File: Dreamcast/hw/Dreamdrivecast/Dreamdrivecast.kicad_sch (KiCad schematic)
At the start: 3 parts

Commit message: More notes about how the dreamcast gdrom protocol works and what the pins do
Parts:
- removed U?: Pico, RPi_Pico:RPi_Pico_SMD_TH, symbol MCU_RaspberryPi_and_Boards:Pico
- added U?: WeAct-RP2040-Pico, WeAct-RP2040-Pico:WeAct-RP2040-Pico, symbol Weact-RP2040-Pico:WeAct-RP2040-Pico
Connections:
- net D0: now also U?.1 (GP0)
- net D1: now also U?.2 (GP1)
- net D10: now also U?.14 (GP10)
- net D11: now also U?.15 (GP11)
- net D12: now also U?.16 (GP12)
- net D13: now also U?.17 (GP13)
- net D14: now also U?.19 (GP14)
- net D15: now also U?.20 (GP15)
- net D2: now also U?.4 (GP2)
- net D3: now also U?.5 (GP3)
- net D4: now also U?.6 (GP4)
- net D5: now also U?.7 (GP5)
- net D6: now also U?.9 (GP6)
- net D7: now also U?.10 (GP7)
- net D8: now also U?.11 (GP8)
- net D9: now also U?.12 (GP9)
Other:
- note added: "(audio data, serial)"
- note added: "33.8688 MHz"
- note added: "Bit clock"
- note added: "DMACK- (DMA acknowledge) (optional) This signal is used by the host in response to DMARQ, for initiating a DMA transfer. DMARQ- (DMA request) (optional) This signal is used for DMA transfer between the host and this device. When data transfer is possible, the device drives the signal. The data transfer direction is controlled by the DIOR- and DIOW- commands. This signal is used in handshaking wit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"
- note added: "D[0:15] Bidirectional data bus that can be used either as 8-bit or 16-bit bus."
- note added: "GD-ROM chip selection"
- note added: "IDE_CSO (Chip select 0) Serves for selecting the command block register. Note: This signal is known as "CS1FX-" in the industry. IDE_CS1(Chip select 1) Serves for selecting the control block register. Note: This signal is known as "CS3FX-" in the industry."
- note added: "INTRQ (Device interrupt) Serves for issuing an interrupt to the host. The INTRQ signal has a hold function which asserts the interrupt only when the device is selected and the host has cleared the nIEN bit in the device control register. When the nIEN bit is "1", or when the device is not selected, the INTRQ signal is in the high-impedance state, regardless of the presence of the hold interrupt. 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"
- note added: "IORDY (I/O channel ready) When the device cannot comply with a data transfer request, the signal is negated in order to expand the register access host transfer cycles. When this signal is driven, it is valid only during the DIOR-/DIOW- cycle for the selected device. When the IORDY signal is not negated, it is in the high- impedance state, because it is an open collector signal."
- note added: "Left right clock"
- note added: "RD (Read strobe signal from the host) At the falling edge of this signal, the data on the DDO- DD7, DD8-DD15 data bus from the device register or data port become valid. At the rising edge of this signal, the host latches on to the data. Until latching is completed, the host cannot access the data."
- note added: "RESET (Device reset) This signal is issued by the host. It is asserted at the start of power-on, and the assert state is maintained until the power supply level has stabilized. This is a tolerance interval until device reset after power-on. MCK (Main clock) 33.8688 MHz clock signal for AICA use. BCLK (Bit clock) Clock signal for fetching Digital Audio. LRCK (Left right clock) Digital Audio left/r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"
- note added: "Specifies the register and data read/write port."
- note added: "WR (Write strobe signal from the host) At the falling edge of this signal, the data on DDO- DD7, DD8-DD15 data bus from the device register or data port are latched. Until latching is completed, the device cannot access the data."
- note removed: "(33MHz)"
- note removed: "(audio data)"
- note removed: "CDDA What pins? Some pins are shared between ide and cdda?"
- note removed: "G1 Bus pins not used by GDRom. Used by Flash Memory?"
- moved on the sheet: CN?, JP?

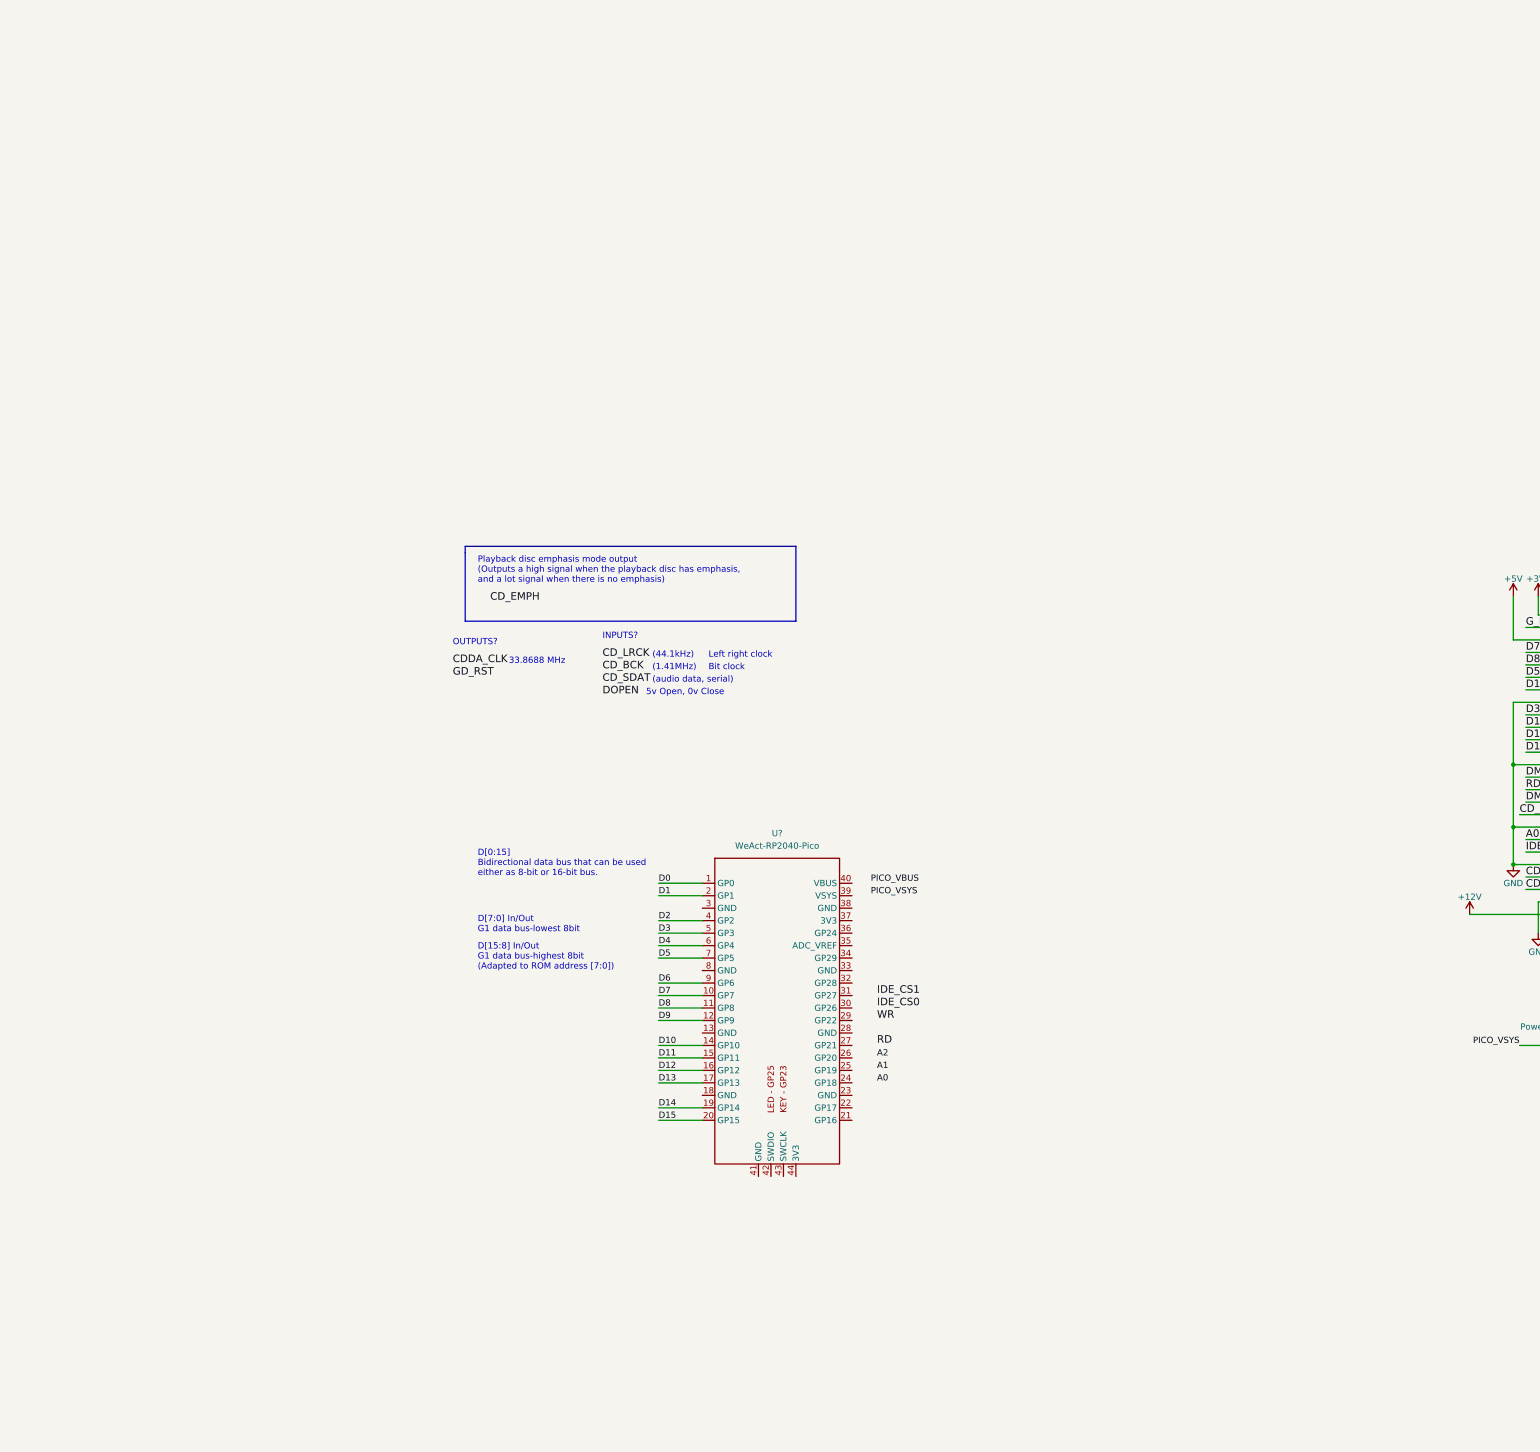
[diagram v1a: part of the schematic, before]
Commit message: Added possible two mcu approach to dreamcast dev board.
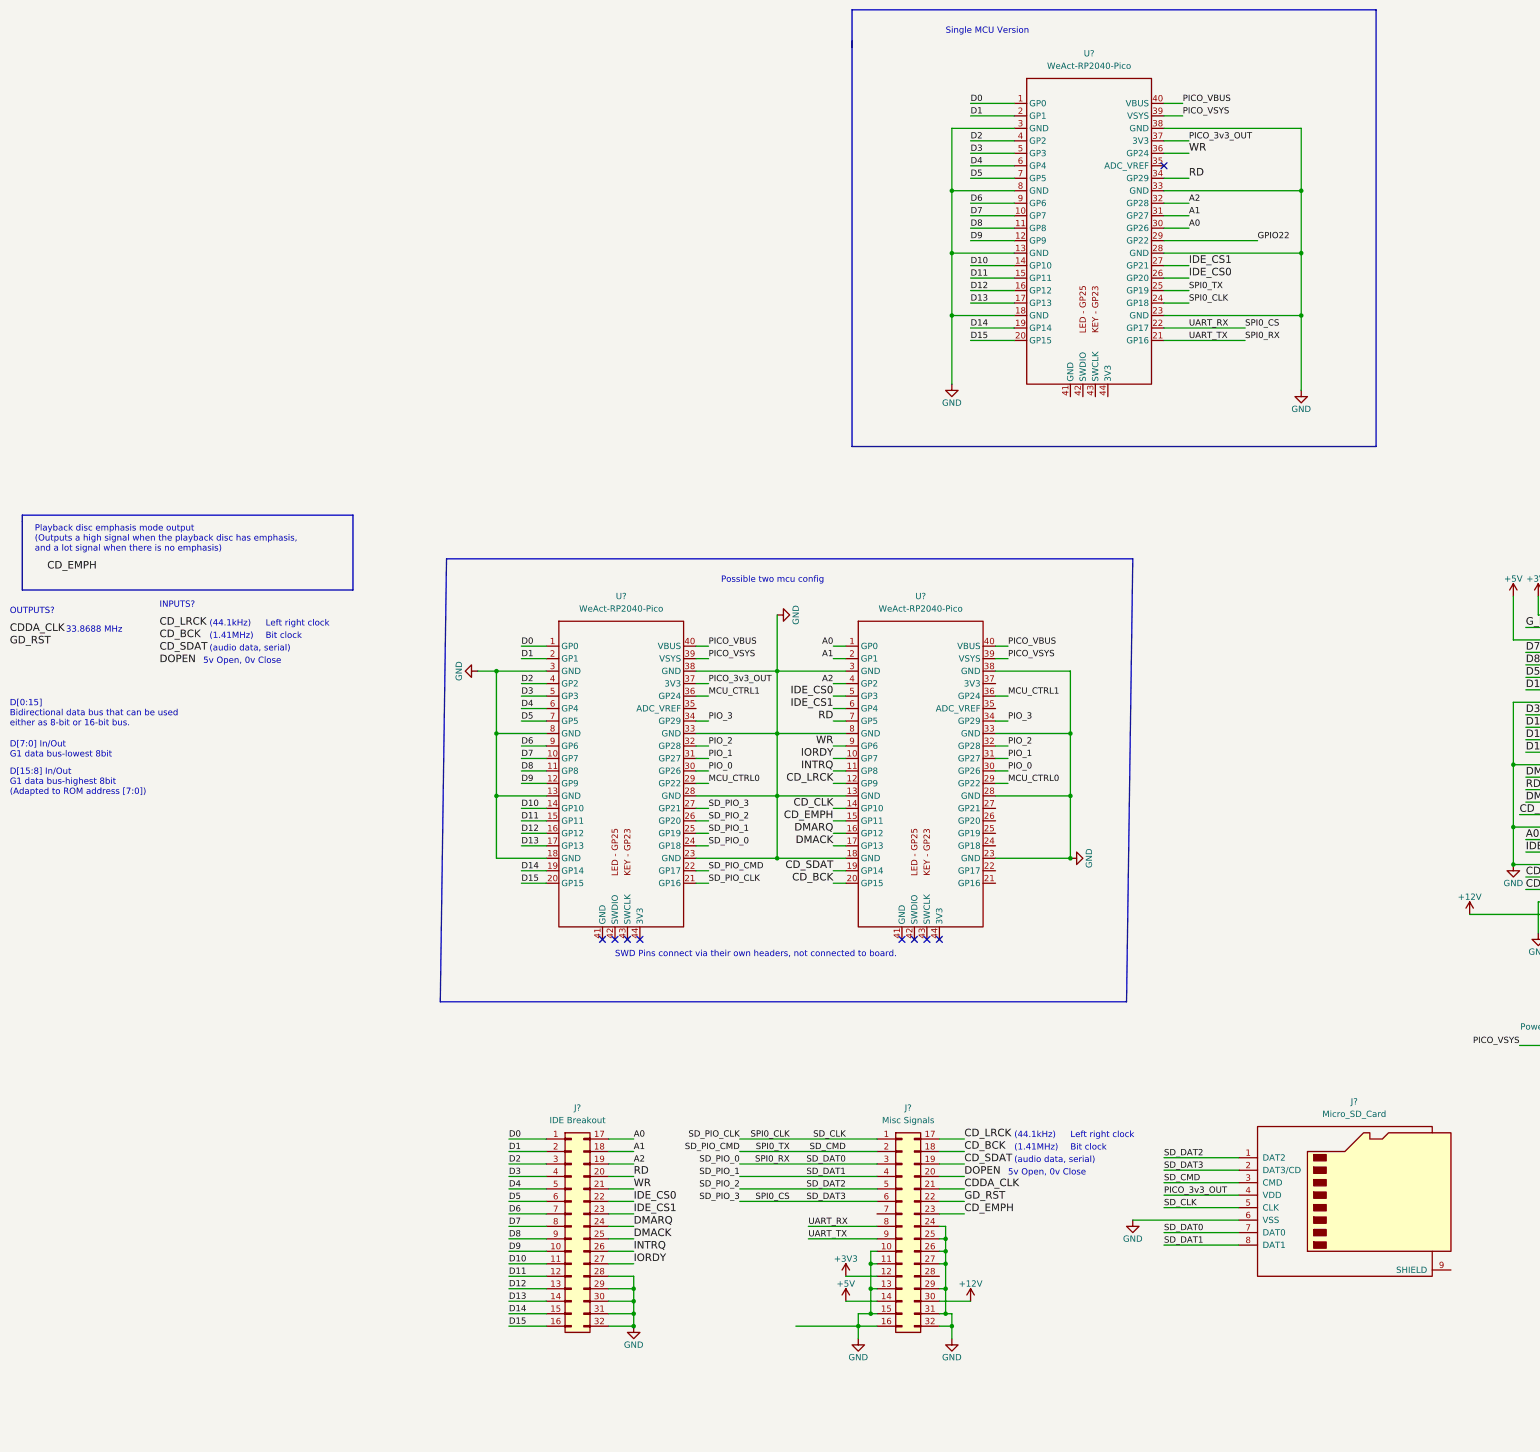
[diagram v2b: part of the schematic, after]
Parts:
- added J?: Misc Signals, symbol Connector_Generic:Conn_02x16_Top_Bottom
- added J?: IDE Breakout, symbol Connector_Generic:Conn_02x16_Top_Bottom
- added J?: Micro_SD_Card, symbol Connector:Micro_SD_Card
- added U? (x2): WeAct-RP2040-Pico, WeAct-RP2040-Pico:WeAct-RP2040-Pico, symbol Weact-RP2040-Pico:WeAct-RP2040-Pico
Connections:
- net +12V: now also J?.30 (Pin_30)
- net +3V3: now also J?.12 (Pin_12)
- net +5V: now also J?.14 (Pin_14)
- net A0: now also U?.30 (GP26), J?.17 (Pin_17), U?.1 (GP0)
- net A1: now also U?.31 (GP27), J?.18 (Pin_18), U?.2 (GP1)
- net A2: now also U?.32 (GP28), J?.19 (Pin_19), U?.4 (GP2)
- net CDDA_CLK: now also J?.21 (Pin_21)
- net CD_BCK: now also J?.18 (Pin_18), U?.20 (GP15)
- net CD_CLK: now also U?.14 (GP10)
- net CD_EMPH: now also J?.23 (Pin_23), U?.15 (GP11)
- net CD_LRCK: now also J?.17 (Pin_17), U?.12 (GP9)
- net CD_SDAT: now also J?.19 (Pin_19), U?.19 (GP14)
- net D0: now also J?.1 (Pin_1), U?.1 (GP0)
- net D1: now also J?.2 (Pin_2), U?.2 (GP1)
- net D10: now also J?.11 (Pin_11), U?.14 (GP10)
- net D11: now also J?.12 (Pin_12), U?.15 (GP11)
- net D12: now also J?.13 (Pin_13), U?.16 (GP12)
- net D13: now also J?.14 (Pin_14), U?.17 (GP13)
- net D14: now also J?.15 (Pin_15), U?.19 (GP14)
- net D15: now also J?.16 (Pin_16), U?.20 (GP15)
- net D2: now also J?.3 (Pin_3), U?.4 (GP2)
- net D3: now also J?.4 (Pin_4), U?.5 (GP3)
- net D4: now also J?.5 (Pin_5), U?.6 (GP4)
- net D5: now also J?.6 (Pin_6), U?.7 (GP5)
- net D6: now also J?.7 (Pin_7), U?.9 (GP6)
- net D7: now also J?.8 (Pin_8), U?.10 (GP7)
- net D8: now also J?.9 (Pin_9), U?.11 (GP8)
- net D9: now also J?.10 (Pin_10), U?.12 (GP9)
- net DMACK: now also J?.25 (Pin_25), U?.17 (GP13)
- net DMARQ: now also J?.24 (Pin_24), U?.16 (GP12)
- net DOPEN: now also J?.20 (Pin_20)
- net GD_RST: now also J?.22 (Pin_22)
- net GND: now also U?.13 (GND), U?.18 (GND), U?.23 (GND), U?.28 (GND), U?.3 (GND), U?.33 (GND), U?.38 (GND), U?.8 (GND), J?.10 (Pin_10), J?.11 (Pin_11), J?.13 (Pin_13), J?.15 (Pin_15), J?.16 (Pin_16), J?.24 (Pin_24), J?.25 (Pin_25), J?.26 (Pin_26), J?.27 (Pin_27), J?.28 (Pin_28), J?.29 (Pin_29), J?.29 (Pin_29), J?.30 (Pin_30), J?.31 (Pin_31), J?.31 (Pin_31), J?.32 (Pin_32), J?.32 (Pin_32), J?.6 (VSS), U?.13 (GND), U?.13 (GND), U?.18 (GND), U?.18 (GND), U?.23 (GND), U?.23 (GND), U?.28 (GND), U?.28 (GND), U?.3 (GND), U?.3 (GND), U?.33 (GND), U?.33 (GND), U?.38 (GND), U?.38 (GND), U?.8 (GND), U?.8 (GND)
- net IDE_CS0: now also U?.26 (GP20), J?.22 (Pin_22), U?.5 (GP3)
- net IDE_CS1: now also U?.27 (GP21), J?.23 (Pin_23), U?.6 (GP4)
- net INTRQ: now also J?.26 (Pin_26), U?.11 (GP8)
- net IORDY: now also J?.27 (Pin_27), U?.10 (GP7)
- net PICO_VBUS: now also U?.40 (VBUS), U?.40 (VBUS), U?.40 (VBUS)
- net PICO_VSYS: now also U?.39 (VSYS), U?.39 (VSYS), U?.39 (VSYS)
- net RD: now also U?.34 (GP29), J?.20 (Pin_20), U?.7 (GP5)
- net WR: now also U?.36 (GP24), J?.21 (Pin_21), U?.9 (GP6)
- net SD_DAT0: now reaches U?.21 (GP16)
- net SD_DAT0: now also J?.3 (Pin_3), J?.7 (DAT0), J?.9 (Pin_9), U?.24 (GP18)
- net SD_DAT3: now reaches U?.22 (GP17)
- net SD_DAT3: now also J?.2 (DAT3/CD), J?.6 (Pin_6), J?.8 (Pin_8), U?.27 (GP21)
- net SD_CLK: now reaches U?.24 (GP18)
- net SD_CLK: now also J?.1 (Pin_1), J?.5 (CLK), U?.21 (GP16)
- net SD_CMD: now reaches U?.25 (GP19)
- net SD_CMD: now also J?.2 (Pin_2), J?.3 (CMD), U?.22 (GP17)
- net GPIO22: now reaches U?.29 (GP22)
- net PICO_3v3_OUT: now reaches U?.37 (3V3)
- net PICO_3v3_OUT: now also J?.4 (VDD), U?.37 (3V3)
- new net MCU_CTRL0: U?.29 (GP22), U?.29 (GP22)
- new net MCU_CTRL1: U?.36 (GP24), U?.36 (GP24)
- new net PIO_0: U?.30 (GP26), U?.30 (GP26)
- new net PIO_1: U?.31 (GP27), U?.31 (GP27)
- new net PIO_2: U?.32 (GP28), U?.32 (GP28)
- new net PIO_3: U?.34 (GP29), U?.34 (GP29)
- new net SD_DAT1: J?.4 (Pin_4), J?.8 (DAT1), U?.25 (GP19)
- new net SD_DAT2: J?.1 (DAT2), J?.5 (Pin_5), U?.26 (GP20)
- no-connect marks 0 -> 9
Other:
- note added: "Possible two mcu config"
- note added: "SWD Pins connect via their own headers, not connected to board."
- note added: "Single MCU Version"
- moved on the sheet: U?

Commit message: Ignore the backup folder. AND also check in the changes to the schematic.
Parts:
- removed U?: WeAct-RP2040-Pico, WeAct-RP2040-Pico:WeAct-RP2040-Pico, symbol Weact-RP2040-Pico:WeAct-RP2040-Pico
- added J?: Ground Block, symbol Connector:Conn_01x16_Male
- added R?: R, Resistor_THT:R_Axial_DIN0207_L6.3mm_D2.5mm_P5.08mm_Vertical, symbol db-passives:R
- added SW?: Lid, symbol Switch:SW_SPST
- JP?: value Power from Dreamcast -> Use Dreamcast Power
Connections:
- net +3V3: now also J?.28 (Pin_28); no longer J?.12 (Pin_12)
- net +5V: now also J?.26 (Pin_26), R?.1; no longer J?.14 (Pin_14)
- net DOPEN: now also R?.2, SW?.2 (B)
- net GND: now also J?.7 (Pin_7), J?.9 (SHIELD), J?.1 (Pin_1), J?.10 (Pin_10), J?.11 (Pin_11), J?.12 (Pin_12), J?.13 (Pin_13), J?.14 (Pin_14), J?.15 (Pin_15), J?.16 (Pin_16), J?.2 (Pin_2), J?.3 (Pin_3), J?.4 (Pin_4), J?.5 (Pin_5), J?.6 (Pin_6), J?.7 (Pin_7), J?.8 (Pin_8), J?.9 (Pin_9), SW?.1 (A); no longer J?.10 (Pin_10), J?.11 (Pin_11), J?.13 (Pin_13), J?.24 (Pin_24), J?.25 (Pin_25), J?.26 (Pin_26), J?.27 (Pin_27), J?.29 (Pin_29), J?.31 (Pin_31)
- net MCU_CTRL0: now also J?.11 (Pin_11)
- net MCU_CTRL1: now also J?.12 (Pin_12)
- net SD_DAT0: no longer J?.9 (Pin_9)
- net SD_DAT3: no longer J?.8 (Pin_8)
- net MCU2_UART_TX: now reaches U?.21 (GP16)
- net MCU2_UART_TX: now also J?.9 (Pin_9)
- net MCU2_UART_RX: now reaches U?.22 (GP17)
- net MCU2_UART_RX: now also J?.8 (Pin_8)
- no-connect marks 9 -> 23
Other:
- note added: "2023-02-16"
- note added: "GDROM Breakout Devboard"
- note added: "GDROM Lid Switch"
- note added: "Power Picos from Dreamcast"
- note removed: "Possible two mcu config"
- note removed: "Single MCU Version"
- moved on the sheet: CN?, J?, JP?, U?

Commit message: Routed dreamcast board. Added some footprints and symbols for the molex connector.
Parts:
- removed J?: Misc Signals, symbol Connector_Generic:Conn_02x16_Top_Bottom
- removed J?: IDE Breakout, symbol Connector_Generic:Conn_02x16_Top_Bottom
- removed J?: Ground Block, symbol Connector:Conn_01x16_Male
- added J1: Breakout, Connector_PinHeader_2.54mm:PinHeader_2x25_P2.54mm_Vertical_SMD, symbol Connector_Generic:Conn_02x25_Top_Bottom
- added J2: POWER, Connector_PinHeader_2.54mm:PinHeader_1x05_P2.54mm_Vertical, symbol Connector:Conn_01x05_Male
- CN1: renamed from CN?; footprint Molex_52602_0579:Molex_52602_0579 -> riser:Molex_52602_0579
- J4: renamed from J?; footprint (none) -> Connector_Card:microSD_HC_Molex_104031-0811
- JP1: renamed from JP?; footprint (none) -> Jumper:SolderJumper-2_P1.3mm_Open_RoundedPad1.0x1.5mm
- SW1: renamed from SW?; footprint (none) -> Button_Switch_THT:SW_DIP_SPSTx01_Slide_9.78x4.72mm_W7.62mm_P2.54mm
- gave numbers to parts that had none: 3
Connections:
- net +12V: now also J2.5 (Pin_5)
- net +3V3: now also J2.4 (Pin_4)
- net +5V: now also J2.3 (Pin_3)
- net A0: now also J1.17 (Pin_17)
- net A1: now also J1.18 (Pin_18)
- net A2: now also J1.19 (Pin_19)
- net CDDA_CLK: now also J1.32 (Pin_32)
- net CD_BCK: now also J1.29 (Pin_29)
- net CD_EMPH: now also J1.34 (Pin_34)
- net CD_LRCK: now also J1.28 (Pin_28)
- net CD_SDAT: now also J1.30 (Pin_30)
- net D0: now also J1.1 (Pin_1)
- net D1: now also J1.2 (Pin_2)
- net D10: now also J1.11 (Pin_11)
- net D11: now also J1.12 (Pin_12)
- net D12: now also J1.13 (Pin_13)
- net D13: now also J1.14 (Pin_14)
- net D14: now also J1.15 (Pin_15)
- net D15: now also J1.16 (Pin_16)
- net D2: now also J1.3 (Pin_3)
- net D3: now also J1.4 (Pin_4)
- net D4: now also J1.5 (Pin_5)
- net D5: now also J1.6 (Pin_6)
- net D6: now also J1.7 (Pin_7)
- net D7: now also J1.8 (Pin_8)
- net D8: now also J1.9 (Pin_9)
- net D9: now also J1.10 (Pin_10)
- net DMACK: now also J1.25 (Pin_25)
- net DMARQ: now also J1.24 (Pin_24)
- net DOPEN: now also J1.31 (Pin_31)
- net GD_RST: now also J1.33 (Pin_33)
- net GND: now also J1.35 (Pin_35), J1.36 (Pin_36), J1.37 (Pin_37), J1.38 (Pin_38), J1.39 (Pin_39), J1.40 (Pin_40), J2.1 (Pin_1); no longer U1.13 (GND), U1.18 (GND), U1.3 (GND), U1.8 (GND), U2.23 (GND), U2.28 (GND), U2.33 (GND), U2.38 (GND)
- net IDE_CS0: now also J1.22 (Pin_22)
- net IDE_CS1: now also J1.23 (Pin_23)
- net INTRQ: now also J1.26 (Pin_26)
- net IORDY: now also J1.27 (Pin_27)
- net MCU2_UART_RX: now also J1.41 (Pin_41)
- net MCU2_UART_TX: now also J1.42 (Pin_42)
- net MCU_CTRL0: now also J1.43 (Pin_43)
- net MCU_CTRL1: now also J1.44 (Pin_44)
- net PICO_3v3_OUT: now also J2.2 (Pin_2)
- net RD: now also J1.20 (Pin_20)
- net SD_CLK: now also J1.45 (Pin_45); no longer U1.21 (GP16)
- net SD_CMD: now also J1.46 (Pin_46); no longer U1.22 (GP17)
- net SD_DAT0: now also J1.47 (Pin_47); no longer U1.24 (GP18)
- net SD_DAT1: now also J1.48 (Pin_48); no longer U1.25 (GP19)
- net SD_DAT2: now also J1.49 (Pin_49); no longer U1.26 (GP20)
- net SD_DAT3: now also J1.50 (Pin_50); no longer U1.27 (GP21)
- net WR: now also J1.21 (Pin_21)
- new net: U1.13 (GND), U1.18 (GND), U1.3 (GND), U1.8 (GND)
- new net: U2.23 (GND), U2.28 (GND), U2.33 (GND), U2.38 (GND)
- new net SD_PIO_0: U1.24 (GP18)
- new net SD_PIO_1: U1.25 (GP19)
- new net SD_PIO_2: U1.26 (GP20)
- new net SD_PIO_3: U1.27 (GP21)
- new net SD_PIO_CLK: U1.21 (GP16)
- new net SD_PIO_CMD: U1.22 (GP17)
- no-connect marks 23 -> 18
